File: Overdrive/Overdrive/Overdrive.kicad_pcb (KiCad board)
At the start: 4 copper layers, 51.5 x 32 mm, 36 parts, among them J1 Conn_02x08_Odd_Even, Q1 2N3904, Q2 2N3904, U2 AD5160, U3 TL071HIDBVR, U4 ADP7118AUJZ-4.5-R7, U5 AD8400ARZ1, U6 TL071HIDBVR

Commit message: overdrive updates to conform with new connector
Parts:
- moved J1 1.56 mm to (205.5, 44.4)
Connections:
- J1 pad 10: /GUITAR_OUT -> /GUITAR_IN
- J1 pad 11: /CS0 -> GND
- J1 pad 12: /MOSI -> GND
- J1 pad 3: GND -> /CS2
- J1 pad 4: GND -> unconnected-(J1-Pin_4-Pad4)
- J1 pad 6: /SPI_CLK -> /CS0
- J1 pad 7: /CS1 -> /MOSI
- J1 pad 8: /GUITAR_IN -> /SPI_CLK
- J1 pad 9: unconnected-(J1-Pin_9-Pad9) -> /GUITAR_OUT
- U2 pad 6: /CS0 -> /CS2
- U5 pad 3: /CS1 -> /CS0
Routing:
- net /CS2: track 0.00 -> 16.8 mm
- net /CS1: track 11.6 -> 0.00 mm, vias 1 -> 0
- net 12V: track 24.8 -> 19.0 mm, vias 8 -> 6
- net /MOSI: track 25.1 -> 30.6 mm, vias 1 -> 2
- net /CS0: track 25.5 -> 20.1 mm, vias 0 -> 2
- net /GUITAR_IN: track 14.4 -> 17.1 mm
- net /SPI_CLK: track 22.2 -> 24.7 mm, vias 1 -> 2
- net GND: track 33.5 -> 35.9 mm, vias 11 -> 19
- net /GUITAR_OUT: track 24.4 -> 22.8 mm

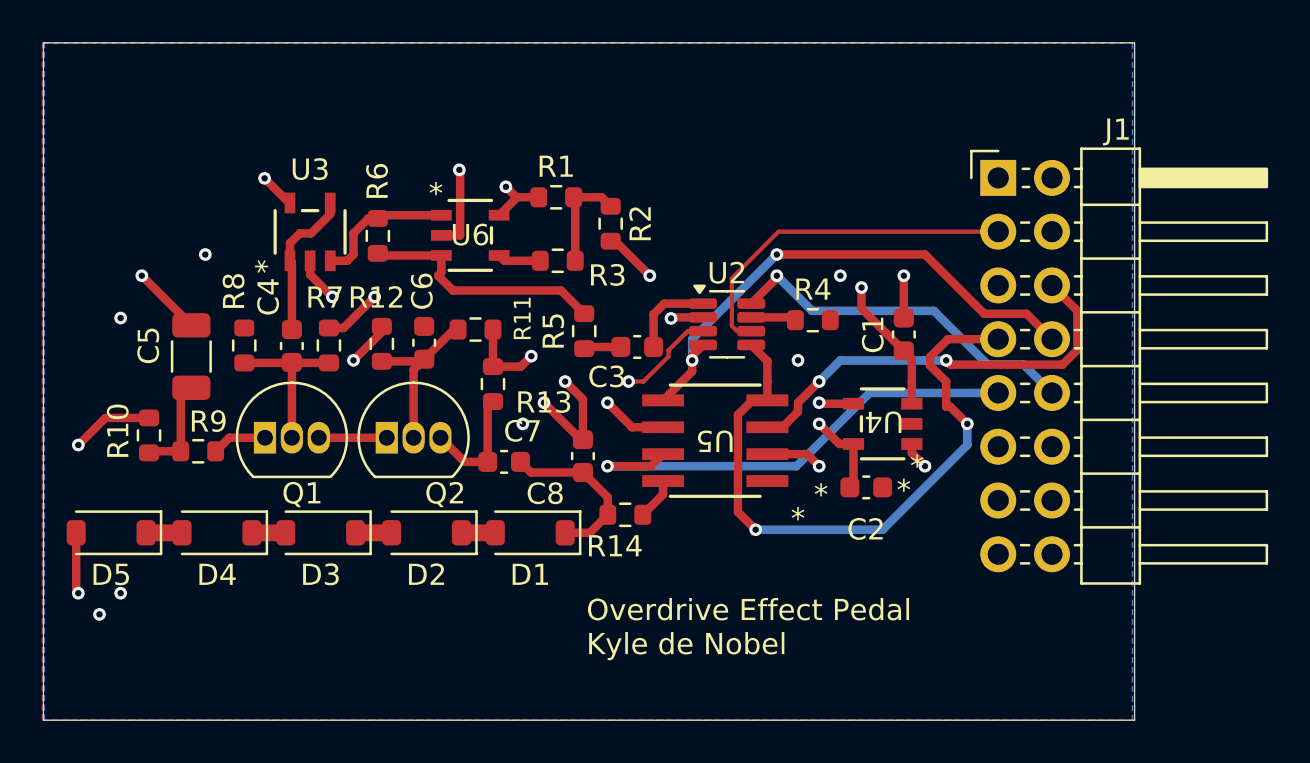
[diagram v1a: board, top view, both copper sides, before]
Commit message: added buffers and caps for op-amps on effect boards
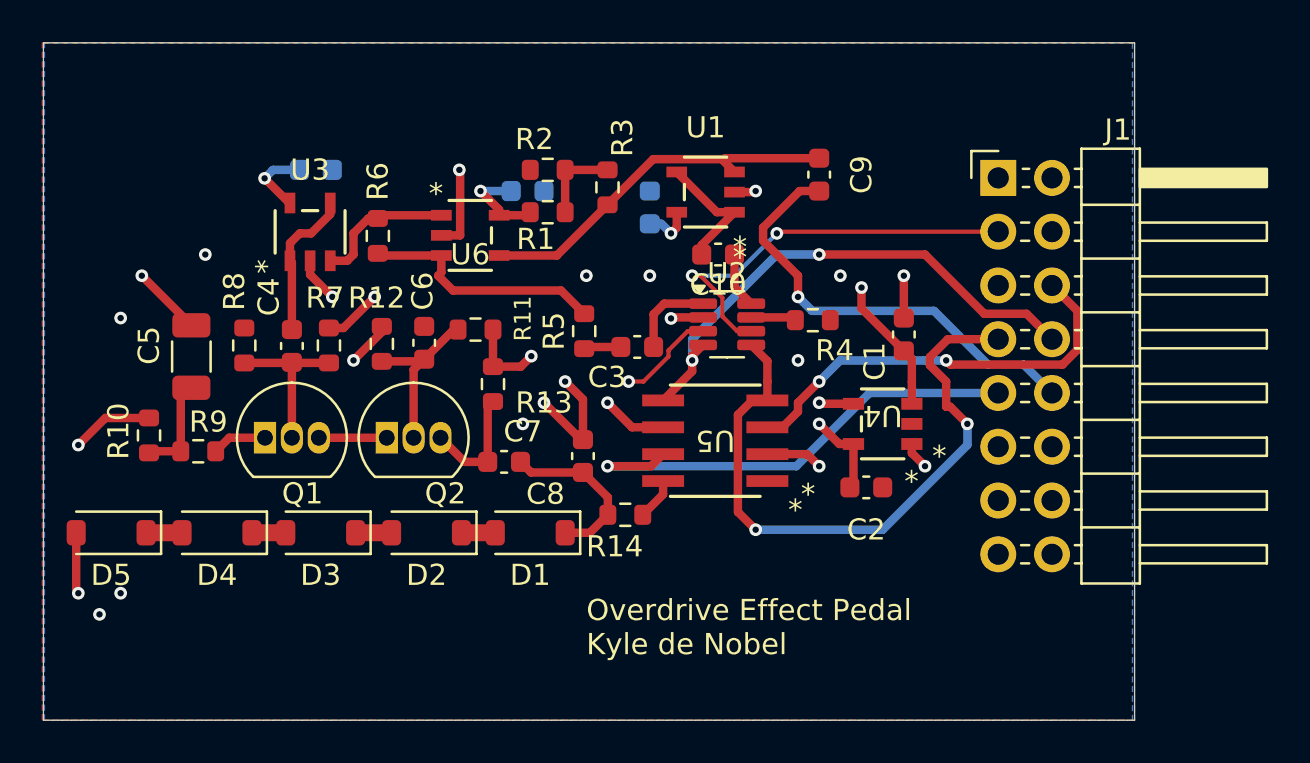
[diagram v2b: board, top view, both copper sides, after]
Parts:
- added C10: 22u, Capacitor_SMD:C_0603_1608Metric, F.Cu at (192.2, 48.0)
- added C11: 1u, Capacitor_SMD:C_0603_1608Metric, B.Cu at (173.2, 44.0)
- added C12: 1u, Capacitor_SMD:C_0603_1608Metric, B.Cu at (183.2, 45.0)
- added C13: 1u, Capacitor_SMD:C_0603_1608Metric, B.Cu at (189.0, 45.8)
- added C9: 1u, Capacitor_SMD:C_0603_1608Metric, F.Cu at (197.0, 44.2)
- added U1: TL071HIDBVR, TL071:TL071HIDBVR, F.Cu at (191.6, 45.0)
- C3: value 0.1u -> 1u
- moved R3 4.19 mm to (187.0, 44.8), turned to 90 degrees
- moved R2 3.92 mm to (184.2, 44.0), turned to 180 degrees
- moved R1 0.81 mm to (184.2, 46.0)
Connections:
- net Net-(U6-IN-) renamed 6V
- U2 pad 8: /GUITAR_IN -> Net-(U2-A)
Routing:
- net 6V: track 2.05 -> 17.9 mm
- net Net-(U1-IN-): track 0.00 -> 6.16 mm
- net 12V: track 19.0 -> 24.6 mm, vias 6 -> 7
- net /GUITAR_IN: track 17.1 -> 21.2 mm
- net /CS2: track 16.8 -> 19.6 mm, vias 0 -> 2
- net Net-(U2-A): track 0.00 -> 2.65 mm
- net GND: track 35.9 -> 34.4 mm, vias 19 -> 21
- net Net-(R1-Pad2): track 4.96 -> 4.00 mm

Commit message: addressed Marco's design review
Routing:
- net GND: track 34.4 -> 26.8 mm
- net 5V: track 10.4 -> 11.1 mm, vias 4 -> 3
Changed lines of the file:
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@@
 		)
 		(fp_text user "*"
-			(at -1.61925 -2.601 0)
+			(at -2.572816 -1.188829 0)
 			(layer "F.SilkS")
 			(effects
@@
 		)
 		(fp_text user "*"
-			(at -1.61925 -2.601 180)
+			(at -1.962696 -1.503324 180)
 			(unlocked yes)
 			(layer "F.SilkS")
@@
 		(tags "capacitor")
 		(property "Reference" "C10"
-			(at 0 -1.43 0)
+			(at 2.866852 -0.103595 0)
 			(layer "F.SilkS")
 			(effects
@@
 		(tags "SOT TO_SOT_SMD")
 		(property "Reference" "U2"
-			(at 0 -2.4 0)
+			(at 1.944203 -2.087528 0)
 			(layer "F.SilkS")
 			(effects
@@
 	)
 	(segment
-		(start 185.840286 54.840286)
-		(end 185 54)
-		(width 0.4)
-		(layer "F.Cu")
-		(net 1)
-	)
-	(segment
-		(start 201 51)
-		(end 201 49)
-		(width 0.4)
-		(layer "F.Cu")
-		(net 1)
-	)
-	(segment
 		(start 172.950001 48.950001)
 		(end 174 50)
@@
 	)
 	(segment
-		(start 185.840286 56.745)
-		(end 185.840286 54.840286)
-		(width 0.4)
-		(layer "F.Cu")
-		(net 1)
-	)
-	(segment
 		(start 193 45.049999)
 		(end 193.950001 45.049999)
@@
 	)
 	(segment
-		(start 185.745 56.745)
-		(end 184 55)
-		(width 0.4)
-		(layer "F.Cu")
-		(net 1)
-	)
-	(segment
 		(start 167.340286 51.340286)
 		(end 165 49)
@@
 	)
 	(via
-		(at 201 49)
-		(size 0.6)
-		(drill 0.3)
-		(layers "F.Cu" "B.Cu")
-		(net 1)
-	)
-	(via
 		(at 165 49)
 		(size 0.6)
@@
 	)
 	(via
+		(at 201.01043 49.394718)
+		(size 0.6)
+		(drill 0.3)
+		(layers "F.Cu" "B.Cu")
+		(free yes)
+		(net 1)
+	)
+	(via
 		(at 198 49)
 		(size 0.6)
@@
 	)
 	(segment
+		(start 197.03846 56.03846)
+		(end 197.03846 55.421446)
+		(width 0.4)
+		(layer "F.Cu")
+		(net 31)
+	)
+	(segment
 		(start 190.05 50.97)
 		(end 190 51.02)
@@
 	)
 	(segment
-		(start 198.62205 55.049999)
-		(end 197.049999 55.049999)
+		(start 198.62205 56.950001)
+		(end 197.950001 56.950001)
 		(width 0.4)
 		(layer "F.Cu")
@@
 	)
 	(segment
-		(start 198.62205 56.950001)
-		(end 197.950001 56.950001)
+		(start 198.62205 55.049999)
+		(end 197.409907 55.049999)
 		(width 0.4)
 		(layer "F.Cu")
@@
 	(segment
 		(start 197.950001 56.950001)
-		(end 197 56)
+		(end 197.03846 56.03846)
 		(width 0.4)
 		(layer "F.Cu")
@@
 	)
 	(segment
-		(start 197.049999 55.049999)
-		(end 197 55)
+		(start 197.409907 55.049999)
+		(end 197.03846 55.421446)
 		(width 0.4)
 		(layer "F.Cu")
@@
 	)
 	(via
-		(at 197 56)
-		(size 0.6)
-		(drill 0.3)
-		(layers "F.Cu" "B.Cu")
-		(net 31)
-	)
-	(via
-		(at 197 55)
+		(at 197.03846 55.421446)
 		(size 0.6)
 		(drill 0.3)
